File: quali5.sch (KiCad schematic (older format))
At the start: 13 parts

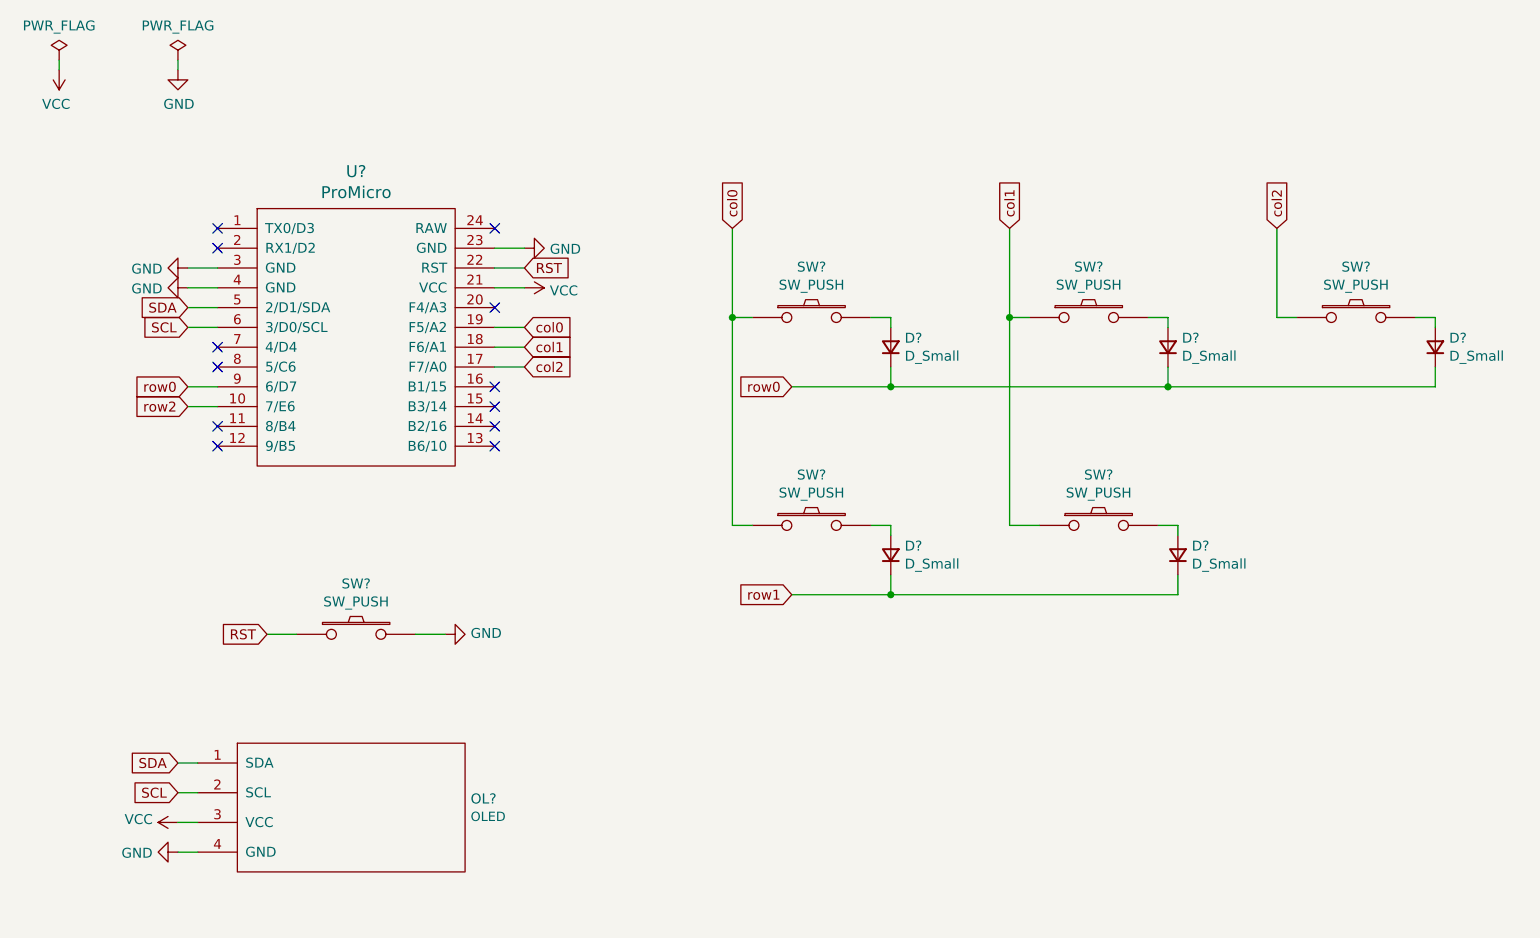
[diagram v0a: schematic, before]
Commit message: Designed PCB footprint
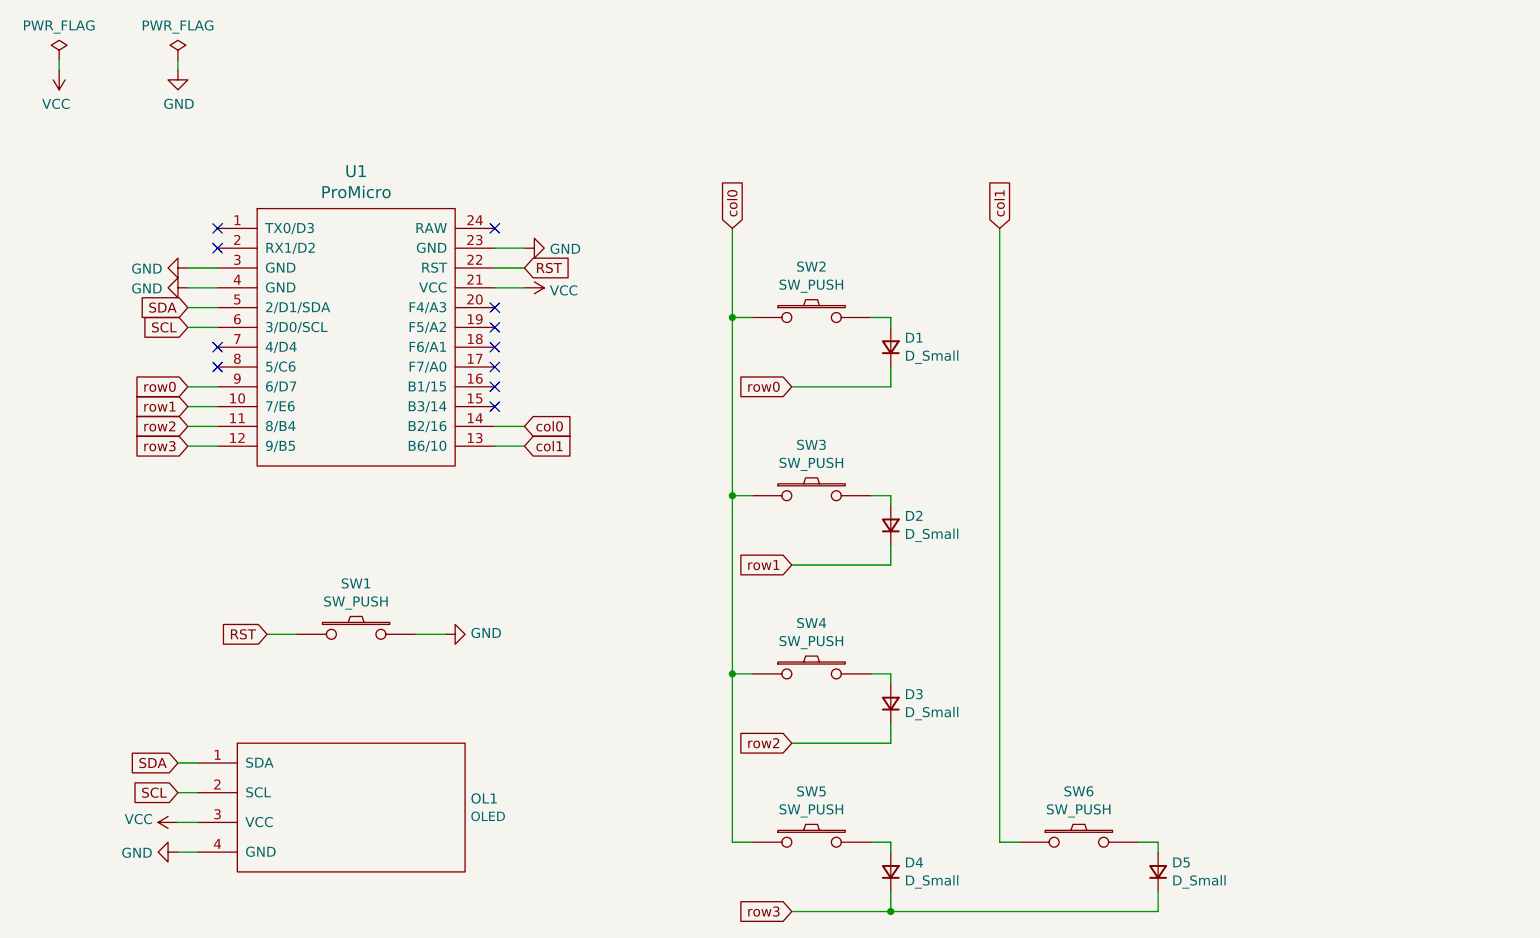
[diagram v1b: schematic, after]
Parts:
- D1, D2, D3, D4, D5: renamed from D?; footprint (none) -> kbd:D3_TH
- OL1: renamed from OL?; footprint (none) -> kbd:OLED
- SW1: renamed from SW?; footprint (none) -> kbd:ResetSW_1side
- SW2, SW3, SW4, SW5, SW6: renamed from SW?; footprint (none) -> kbd:ChocV1_V2_Hotswap
- U1: renamed from U?; footprint (none) -> kbd:ProMicro_v3.5
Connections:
- net col0: now also SW4.1, SW5.1, U1.14 (B2/16); no longer U1.19 (F5/A2)
- net col1: now also SW6.1, U1.13 (B6/10); no longer SW4.1, SW5.1, U1.18 (F6/A1)
- net row0: no longer D3.1 (K), D5.1 (K)
- net row1: now also U1.10 (7/E6); no longer D4.1 (K)
- net row2: now also D3.1 (K), U1.11 (8/B4); no longer U1.10 (7/E6)
- net row3: now reaches U1.12 (9/B5)
- net row3: now also D4.1 (K), D5.1 (K)
- net col2: no longer names the net of U1.17 (F7/A0)
- net col2: no longer SW6.1
- no-connect marks 12 -> 11
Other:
- moved on the sheet: D2, D3, D4, D5, SW3, SW4, SW5, SW6

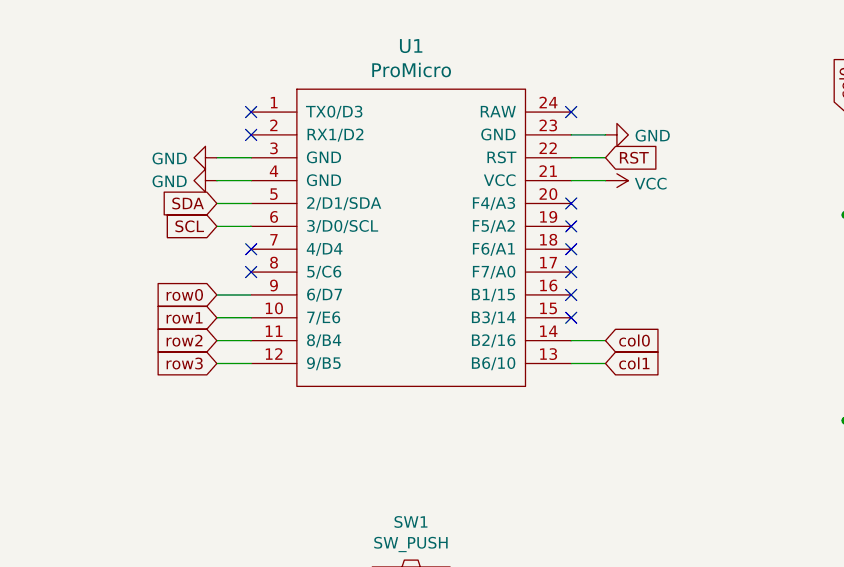
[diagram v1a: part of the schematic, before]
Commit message: Update PCB for rev.2
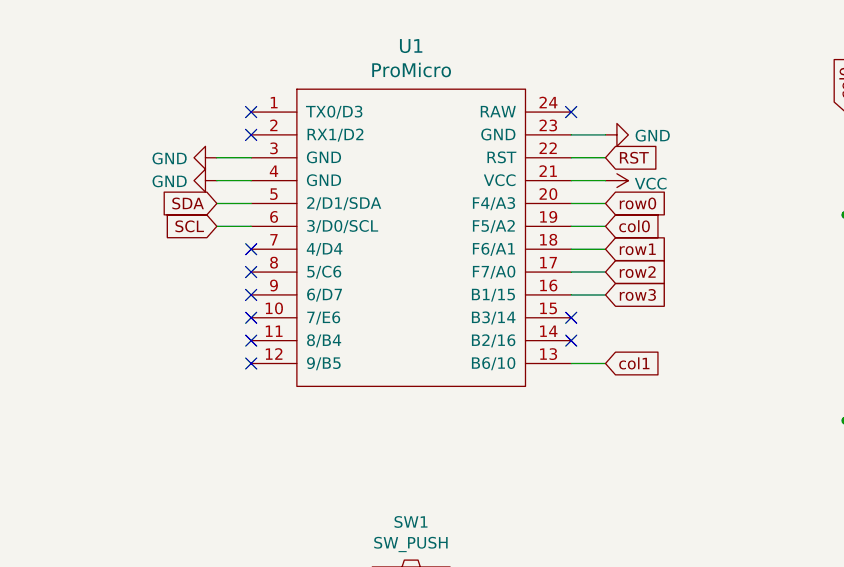
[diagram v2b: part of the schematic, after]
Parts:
- D1, D2, D3, D4, D5: footprint kbd:D3_TH -> kbd:D3_SMD
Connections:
- net col0: now also U1.19 (F5/A2); no longer U1.14 (B2/16)
- net row0: now also U1.20 (F4/A3); no longer U1.9 (6/D7)
- net row1: now also U1.18 (F6/A1); no longer U1.10 (7/E6)
- net row2: now also U1.17 (F7/A0); no longer U1.11 (8/B4)
- net row3: now also U1.16 (B1/15); no longer U1.12 (9/B5)
